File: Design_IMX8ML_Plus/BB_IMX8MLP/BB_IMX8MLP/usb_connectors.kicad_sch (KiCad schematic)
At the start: 36 parts, among them J14 USB_C_Receptacle, J9 GSB311231HR, U10 PCMF3USB3S, U40 PCMF3USB3S, U9 PCMF3USB3S

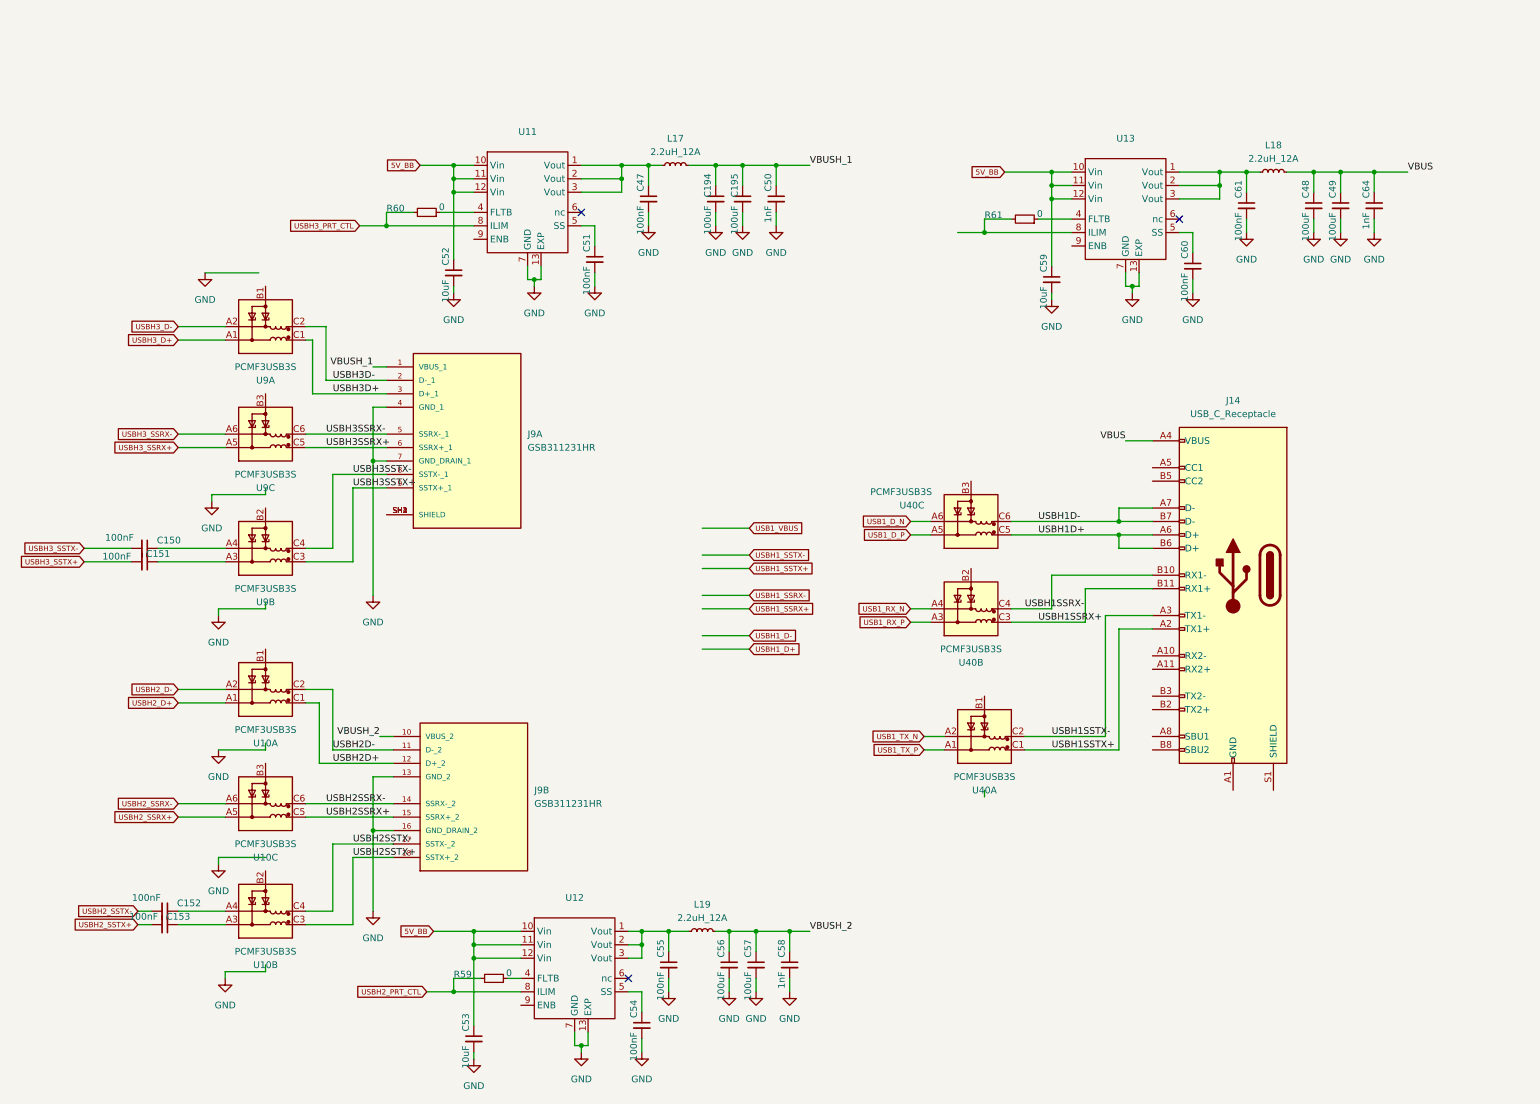
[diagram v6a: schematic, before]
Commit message: [BB_IMX8MLP IMX8MLP] Actuallizated to 9.0 kicad version
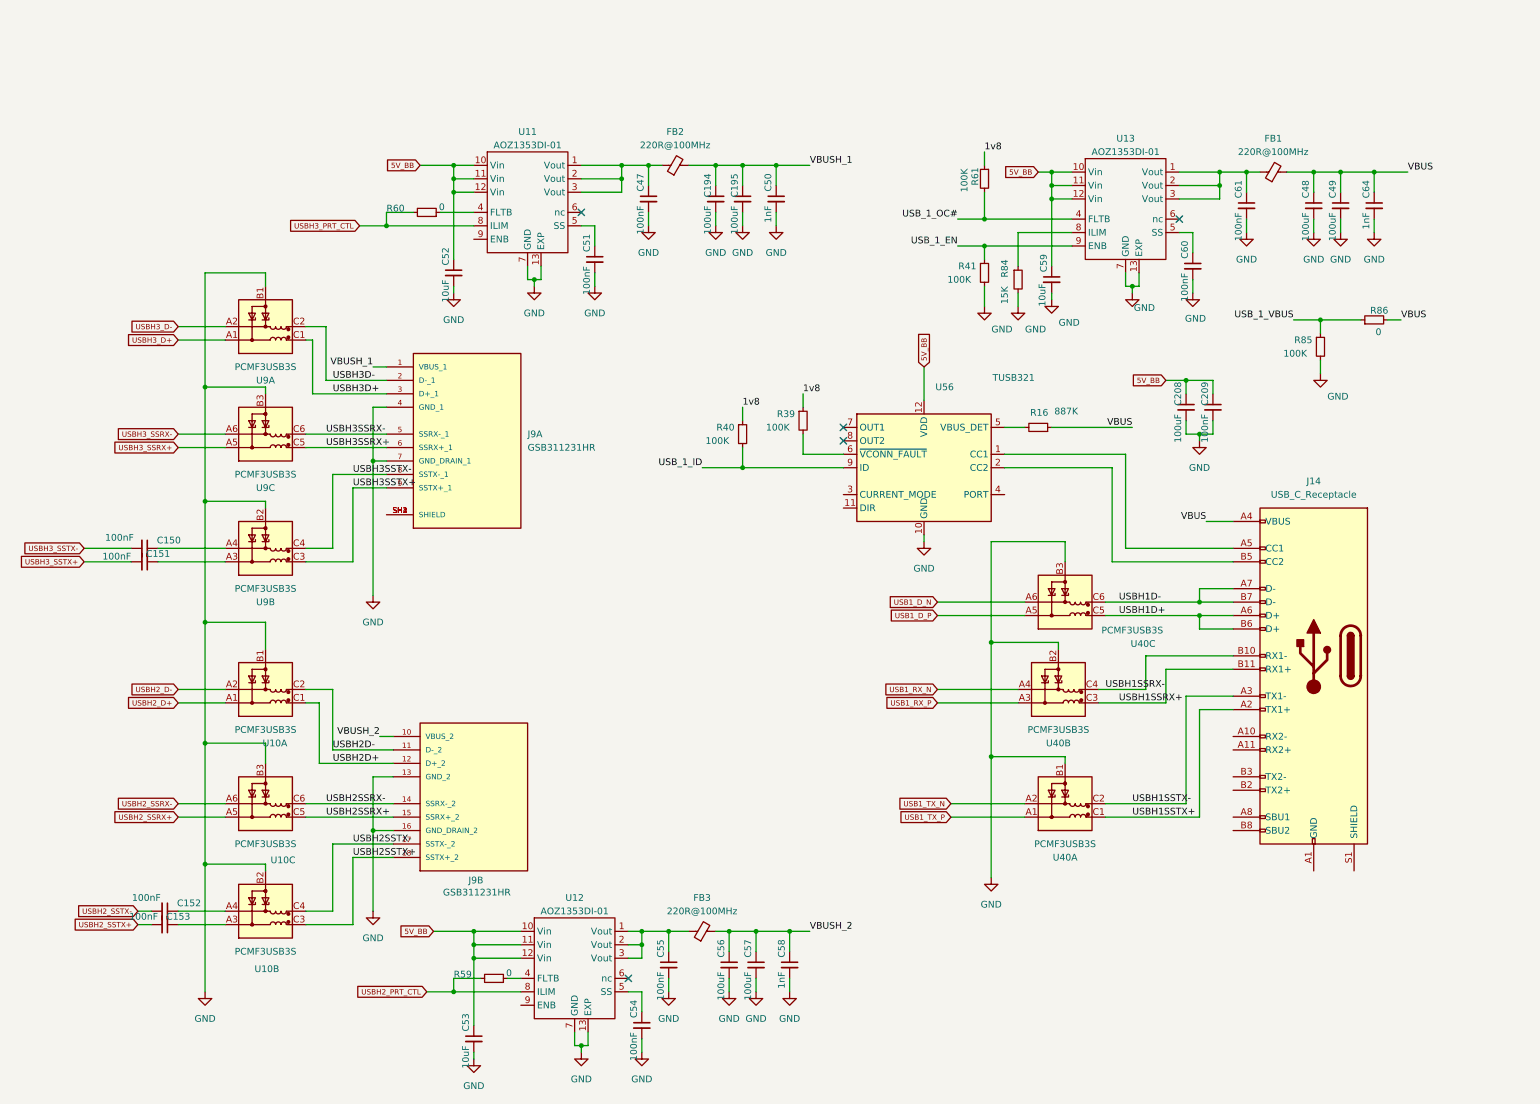
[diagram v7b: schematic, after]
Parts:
- removed L17, L18, L19: 2.2uH_12A, Inductor_SMD:L_1806_4516Metric, symbol Device:L_Small
- added C208: 100uF, Capacitor_SMD:C_1210_3225Metric, symbol Device:C_Small
- added C209: 100nF, Capacitor_SMD:C_0402_1005Metric, symbol Device:C_Small
- added FB1, FB2, FB3: 220R@100MHz, Inductor_SMD:L_0603_1608Metric, symbol Device:FerriteBead_Small
- added R16: 887K, Resistor_SMD:R_0402_1005Metric, symbol Device:R_Small
- added R39, R40, R41, R85: 100K, Resistor_SMD:R_0402_1005Metric, symbol Device:R_Small
- added R84: 15K, Resistor_SMD:R_0402_1005Metric, symbol Device:R_Small
- added R86: 0, Resistor_SMD:R_0402_1005Metric, symbol Device:R_Small
- added U56: TUSB321, Package_DFN_QFN:Texas_X2QFN-12_1.6x1.6mm_P0.4mm, symbol Interface_USB:TUSB321
- C150, C151, C152, C153, C47, C51, C54, C55, C60, C61: MP (none) -> C0402C104K4RACTU; Price (none) -> 0.1
- C194, C195, C48, C49, C56, C57: footprint Capacitor_SMD:C_1210_3225Metric_Pad1.33x2.70mm_HandSolder -> Capacitor_SMD:C_1210_3225Metric; MP (none) -> GRM32ER61A107ME20K; Price (none) -> 1
- C50, C58, C64: MP (none) -> C0402C102K5RECTU; Price (none) -> 0.1
- C52, C53, C59: footprint Capacitor_SMD:C_0603_1608Metric_Pad1.08x0.95mm_HandSolder -> Capacitor_SMD:C_0603_1608Metric; MP (none) -> LMK107BBJ106MALT; Price (none) -> 0.1
- J14: MP (none) -> 1054500101; Price (none) -> 3
- J9: Price None -> 3.5
- R59, R60: MP (none) -> CRCW04020000Z0ED; Price (none) -> 0.1
- R61: value 0 -> 100K; MP (none) -> CRCW04020000Z0ED; Price (none) -> 0.1
- U10, U40, U9: MP (none) -> PCMF3USB3SZ; Price (none) -> 1.5
- U11, U12, U13: value ~ -> AOZ1353DI-01; MP (none) -> AOZ1353DI-01; Price (none) -> 1.5
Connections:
- net 5V_BB: now also C208.1, C209.1, U56.12 (VDD)
- net GND: now also U10.B1 (GND_CH1), U10.B2 (GND_CH2), U10.B3 (GND_CH3), U40.B1 (GND_CH1), U40.B2 (GND_CH2), U40.B3 (GND_CH3), U9.B1 (GND_CH1), U9.B2 (GND_CH2), U9.B3 (GND_CH3), C208.2, C209.2, R41.2, R84.2, R85.2, U56.10 (GND)
- net VBUS: now also FB1.2, R16.1, R86.2
- net VBUSH_1: now also FB2.2
- net VBUSH_2: now also FB3.2
- net at C55.1, U12.1 (Vout), U12.2 (Vout)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: now also FB3.1
- net at C47.1, U11.1 (Vout), U11.2 (Vout)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: now also FB2.1
- net at C61.1, U13.1 (Vout), U13.2 (Vout)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: now also FB1.1
- net at J14.A5 (CC1): now also U56.1 (CC1)
- net at J14.B5 (CC2): now also U56.2 (CC2)
- net 1v8: now reaches R61.1
- net 1v8: now also R39.1, R40.1; no longer U13.4 (FLTB)
- net at U13.8 (ILIM): now also R84.1; no longer R61.2
- net USB_1_EN: now reaches U13.9 (ENB)
- net USB_1_EN: now also R41.1
- new net: R16.2, U56.5 (VBUS_DET)
- new net: R39.2, U56.6 (~{VCONN_FAULT})
- new net USB_1_ID: R40.2, U56.9 (ID)
- new net USB_1_OC#: R61.2, U13.4 (FLTB)
- new net USB_1_VBUS: R85.1, R86.1
- no-connect marks 3 -> 5
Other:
- moved on the sheet: J14, R61, U40A, U40B, U40C
